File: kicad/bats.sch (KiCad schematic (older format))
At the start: 36 parts, among them P1 SERVO, SW1 UP, SW2 LEFT, SW3 DOWN, SW4 RIGHT, SW5 RESET, SW6 UP, SW7 LEFT, SW8 DOWN, SW9 RIGHT, U1 BUZZER

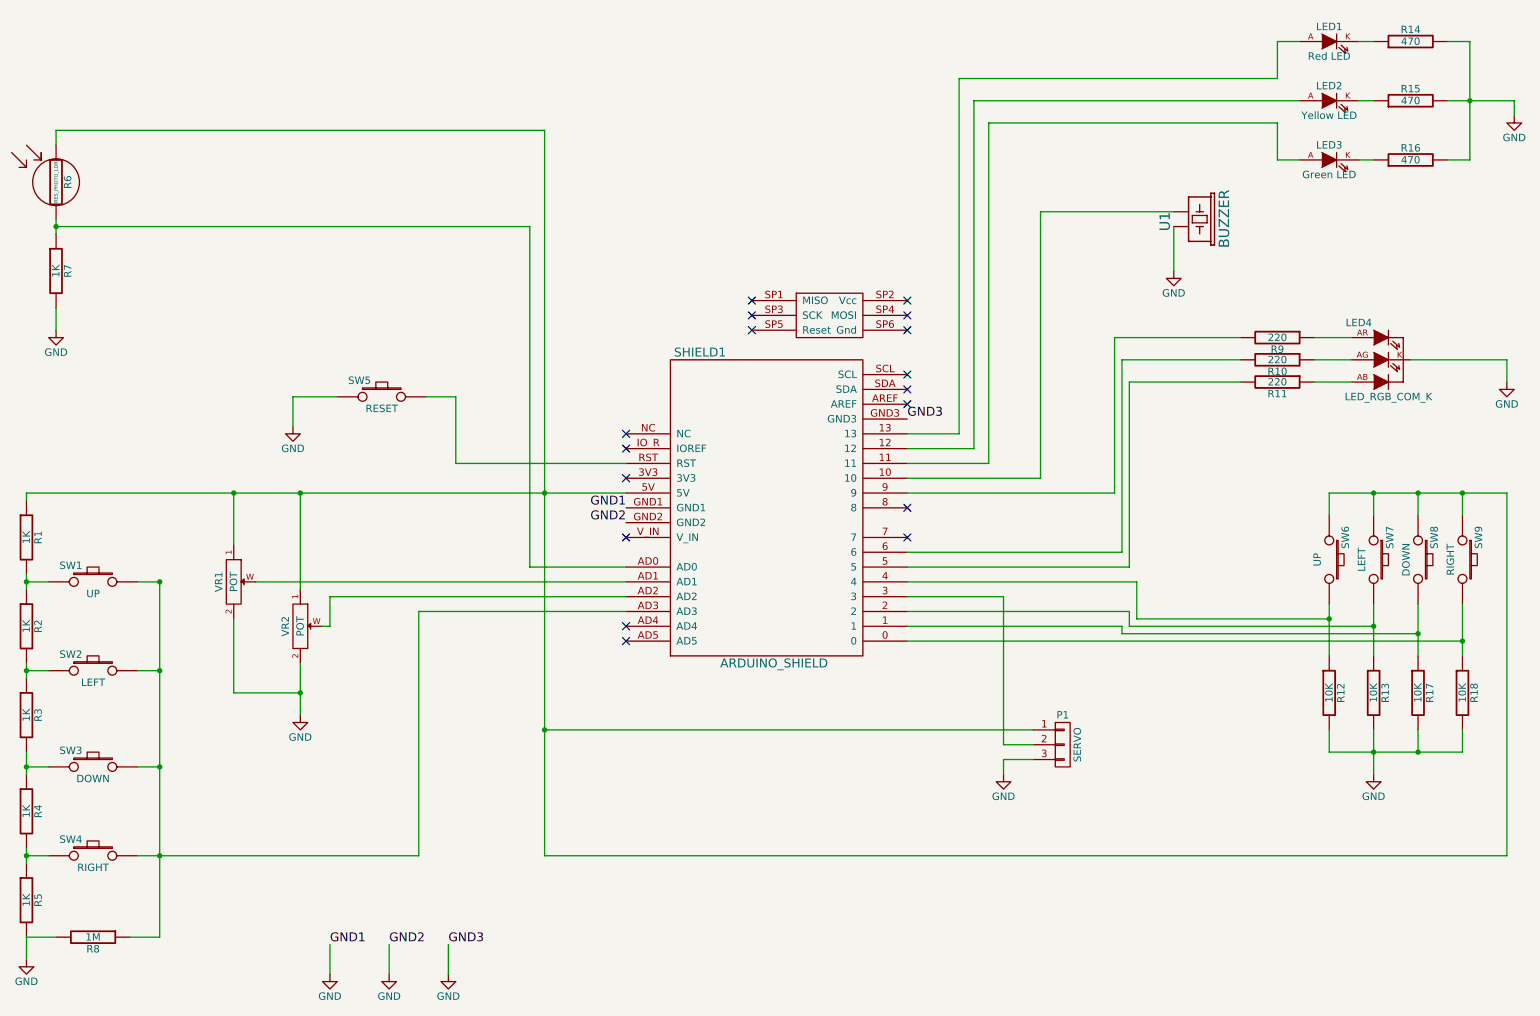
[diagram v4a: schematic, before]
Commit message: Cambiado o footprint dos potes. Todos os compoñentes situados na placa Mínimos cambios na documentación (engadida breve explicación dos submódulos de git)
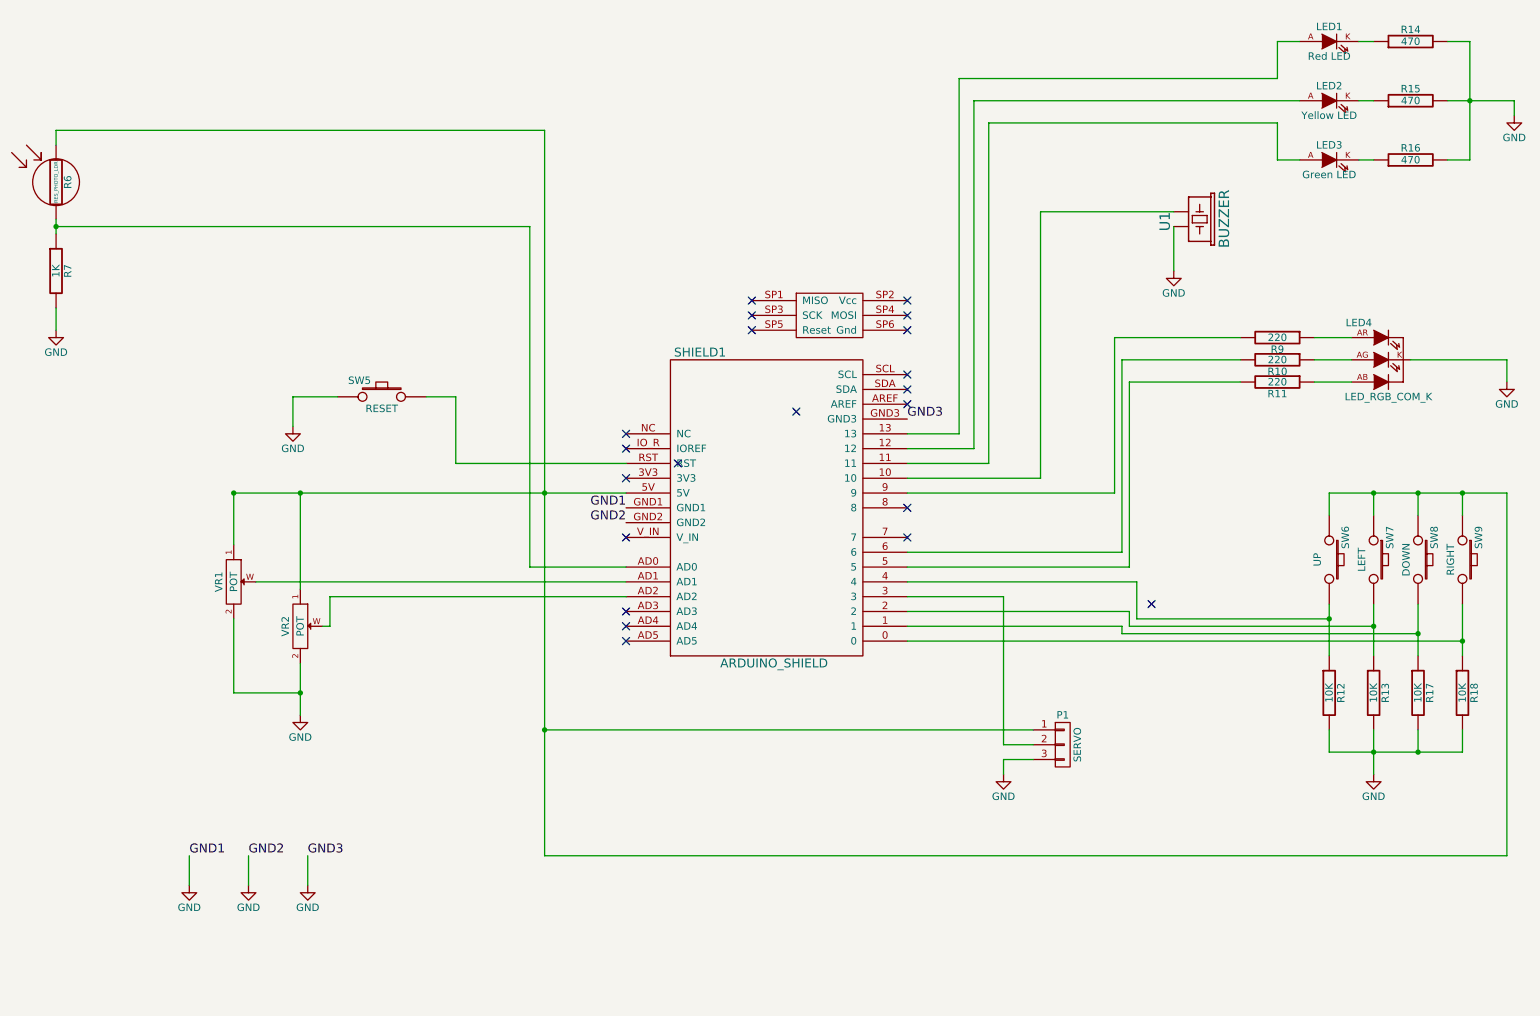
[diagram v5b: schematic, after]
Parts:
- removed R1, R2, R3, R4, R5: 1K, Resistors_ThroughHole:Resistor_Horizontal_RM10mm, symbol R
- removed R8: 1M, Resistors_ThroughHole:Resistor_Horizontal_RM10mm, symbol R
- removed SW1: UP, FT:SW_PUSHBUTTON_PTH, symbol SW_PUSHBUTTON
- removed SW2: LEFT, FT:SW_PUSHBUTTON_PTH, symbol SW_PUSHBUTTON
- removed SW3: DOWN, FT:SW_PUSHBUTTON_PTH, symbol SW_PUSHBUTTON
- removed SW4: RIGHT, FT:SW_PUSHBUTTON_PTH, symbol SW_PUSHBUTTON
- U1: footprint Buzzers_Beepers:MagneticBuzzer_StarMicronics_HMB-06_HMB-12 -> Buzzers_Beepers:MagneticBuzzer_Kingstate_KCG0601
- VR1, VR2: footprint (none) -> FT:POT_RV09_VERT
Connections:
- no-connect marks 17 -> 21

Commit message: Engadida unha "KiCAD cheat sheet", una chuleta para KiCAD, non rematada
Engadida unha segunda versión da placa intentando deixar todo nunha
cara.
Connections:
- no-connect marks 21 -> 18
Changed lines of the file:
@@
 $EndDescr
-$Comp
-L ARDUINO_SHIELD SHIELD1
-U 1 1 55897B99
-P 5800 4050
-F 0 "SHIELD1" H 5350 5200 60  0000 C CNN
-F 1 "ARDUINO_SHIELD" H 5850 3100 60  0000 C CNN
-F 2 "FT:ARDUINO_SHIELD" H 5800 3850 50  0001 C CNN
-F 3 "" H 5800 4050 60  0000 C CNN
-	1    5800 4050
-	1    0    0    -1
-$EndComp
 $Comp
 L LED LED3
@@
 $EndComp
 NoConn ~ 4850 4650
-NoConn ~ 8400 4600
-NoConn ~ 6000 3300
-NoConn ~ 5200 3650
+$Comp
+L ARDUINO_SHIELD SHIELD1
+U 1 1 55897B99
+P 5800 4050
+F 0 "SHIELD1" H 5350 5200 60  0000 C CNN
+F 1 "ARDUINO_SHIELD" H 5850 3100 60  0000 C CNN
+F 2 "FT:ARDUINO_SHIELD" H 5800 3850 50  0001 C CNN
+F 3 "" H 5800 4050 60  0000 C CNN
+	1    5800 4050
+	1    0    0    -1
+$EndComp
 $EndSCHEMATC

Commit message: Un commit intermedio facendo probas
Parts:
- added R1: 10K, Resistors_ThroughHole:Resistor_Horizontal_RM10mm, symbol R
- added SW1: SHOT, FT:SW_PUSHBUTTON_PTH, symbol SW_PUSHBUTTON
- renumbered SW5 to SW0, SW6 to SW2, SW7 to SW3, SW8 to SW4, SW9 to SW5
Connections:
- net GND: now also R1.2
- net ARD4: now reaches R18.1, SW5.2
- net ARD4: now also SHIELD1.4; no longer SHIELD1.0
- net ARD3: now reaches R17.1, SW4.2
- net ARD3: now also SHIELD1.3; no longer SHIELD1.1
- net ARD10: now reaches SHIELD1.10
- net ARD10: now also R10.2; no longer U1.2 (GND)
- net ARD11: now reaches SHIELD1.11
- net ARD11: now also R9.2; no longer LED3.A
- net at SHIELD1.12: no longer LED2.A
- net ARD13: now reaches SHIELD1.13
- net ARD13: now also U1.2 (GND); no longer LED1.A
- net ARD2: now reaches R13.1, SHIELD1.2, SW3.2
- net ARD5: now reaches P1.2 (P2)
- net ARD5: now also SHIELD1.5; no longer SHIELD1.3
- net ARD1: now reaches R12.1, SW2.2
- net ARD1: now also SHIELD1.1; no longer SHIELD1.4
- net ARD9: now reaches R11.2
- net ARD9: now also SHIELD1.9; no longer SHIELD1.5
- net at P1.1 (P1), R6.1, SHIELD1.5V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: now also SW1.1
- net ARD6: now reaches SHIELD1.6
- net ARD6: now also LED3.A; no longer R10.2
- net ARD7: now reaches SHIELD1.7
- net ARD7: now also LED2.A
- net ARD8: now reaches SHIELD1.8
- net ARD8: now also LED1.A
- new net ARD0: R1.1, SHIELD1.0, SW1.2
- no-connect marks 18 -> 17
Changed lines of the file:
@@
-$EndComp
-$Comp
-L SW_PUSHBUTTON SW6
-U 1 1 5589867E
-P 9600 4300
-F 0 "SW6" H 9450 4410 50  0000 C CNN
-F 1 "UP" H 9600 4220 50  0000 C CNN
-F 2 "FT:SW_PUSHBUTTON_PTH" H 9600 4300 60  0001 C CNN
-F 3 "" H 9600 4300 60  0000 C CNN
-	1    9600 4300
-	0    1    1    0
 $EndComp
 $Comp
@@
 $EndComp
 $Comp
-L SW_PUSHBUTTON SW7
+L SW_PUSHBUTTON SW3
 U 1 1 558AEB11
 P 9900 4300
-F 0 "SW7" H 9750 4410 50  0000 C CNN
+F 0 "SW3" H 9750 4410 50  0000 C CNN
 F 1 "LEFT" H 9900 4220 50  0000 C CNN
 F 2 "FT:SW_PUSHBUTTON_PTH" H 9900 4300 60  0001 C CNN
@@
 $EndComp
 $Comp
-L SW_PUSHBUTTON SW8
+L SW_PUSHBUTTON SW4
 U 1 1 558AEBB0
 P 10200 4300
-F 0 "SW8" H 10050 4410 50  0000 C CNN
+F 0 "SW4" H 10050 4410 50  0000 C CNN
 F 1 "DOWN" H 10200 4220 50  0000 C CNN
 F 2 "FT:SW_PUSHBUTTON_PTH" H 10200 4300 60  0001 C CNN
@@
 $EndComp
 $Comp
-L SW_PUSHBUTTON SW9
+L SW_PUSHBUTTON SW5
 U 1 1 558AEBBD
 P 10500 4300
-F 0 "SW9" H 10350 4410 50  0000 C CNN
+F 0 "SW5" H 10350 4410 50  0000 C CNN
 F 1 "RIGHT" H 10500 4220 50  0000 C CNN
 F 2 "FT:SW_PUSHBUTTON_PTH" H 10500 4300 60  0001 C CNN
@@
 $EndComp
 $Comp
-L SW_PUSHBUTTON SW5
+L SW_PUSHBUTTON SW0
 U 1 1 558B73E7
 P 3200 3200
-F 0 "SW5" H 3050 3310 50  0000 C CNN
+F 0 "SW0" H 3050 3310 50  0000 C CNN
 F 1 "RESET" H 3200 3120 50  0000 C CNN
 F 2 "FT:SW_PUSHBUTTON_PTH" H 3200 3200 60  0001 C CNN
@@
 	1    0    0    -1
 $EndComp
-NoConn ~ 6750 3950
-NoConn ~ 6750 4150
 NoConn ~ 4850 4750
 NoConn ~ 4850 4850
@@
 Connection ~ 10550 1200
 Wire Wire Line
-	9400 1600 9250 1600
-Wire Wire Line
-	7100 1050 7100 3450
-Wire Wire Line
-	7100 3450 6750 3450
-Wire Wire Line
-	7200 1200 9400 1200
-Wire Wire Line
-	7200 1200 7200 3550
-Wire Wire Line
-	7200 3550 6750 3550
-Wire Wire Line
-	7300 1350 7300 3650
-Wire Wire Line
-	7300 3650 6750 3650
-Wire Wire Line
 	1000 2600 1000 2750
 Wire Wire Line
@@
 Wire Wire Line
 	1000 1400 1000 1500
-Wire Wire Line
-	7650 1950 8550 1950
 Wire Wire Line
 	8550 2050 8550 2350
@@
 Connection ~ 10500 3850
 Wire Wire Line
-	9600 3850 10800 3850
+	9300 3850 10800 3850
 Wire Wire Line
 	9600 3850 9600 4000
-Connection ~ 9600 4700
-Connection ~ 9900 4750
-Connection ~ 10200 4800
-Connection ~ 10500 4850
 Wire Wire Line
 	9600 5450 9600 5600
 Wire Wire Line
-	9600 5600 10500 5600
+	9300 5600 10500 5600
 Wire Wire Line
 	10500 5600 10500 5450
@@
 Connection ~ 10200 5600
 Wire Wire Line
-	10500 4850 6750 4850
-Wire Wire Line
-	8200 4800 10200 4800
-Wire Wire Line
-	8200 4800 8200 4750
-Wire Wire Line
-	8200 4750 6750 4750
-Wire Wire Line
-	9900 4750 8250 4750
-Wire Wire Line
-	8250 4750 8250 4650
-Wire Wire Line
-	8250 4650 6750 4650
-Wire Wire Line
-	8300 4700 9600 4700
-Wire Wire Line
-	8300 4450 8300 4700
-Wire Wire Line
-	7300 1350 9250 1350
-Wire Wire Line
-	9250 1350 9250 1600
-Wire Wire Line
-	7100 1050 9250 1050
-Wire Wire Line
-	9250 1050 9250 800
-Wire Wire Line
-	9250 800  9400 800
-Wire Wire Line
 	9500 2800 9750 2800
 Wire Wire Line
@@
 Wire Wire Line
 	10850 1200 10850 1300
-Wire Wire Line
-	6750 3750 7650 3750
-Wire Wire Line
-	7650 3750 7650 1950
-Wire Wire Line
-	6750 3850 8150 3850
-Wire Wire Line
-	8150 3850 8150 2800
-Wire Wire Line
-	8150 2800 9000 2800
-Wire Wire Line
-	9000 2950 8200 2950
-Wire Wire Line
-	8200 2950 8200 4250
-Wire Wire Line
-	8200 4250 6750 4250
-Wire Wire Line
-	6750 4350 8250 4350
-Wire Wire Line
-	8250 4350 8250 3100
-Wire Wire Line
-	8250 3100 9000 3100
-Wire Wire Line
-	6750 4450 8300 4450
-Wire Wire Line
-	6750 4550 7400 4550
-Wire Wire Line
-	7400 4550 7400 5550
 Wire Wire Line
 	7400 5550 7600 5550
@@
 	1    0    0    -1
 $EndComp
+Wire Wire Line
+	8550 1950 8250 1950
+Text Label 8250 1950 2    60   ~ 0
+ARD13
+Text Label 6750 3450 0    60   ~ 0
+ARD13
+Wire Wire Line
+	9400 800  9000 800
+Wire Wire Line
+	9400 1200 9000 1200
+Wire Wire Line
+	9400 1600 9000 1600
+Text Label 6750 3650 0    60   ~ 0
+ARD11
+Text Label 6750 3750 0    60   ~ 0
+ARD10
+Text Label 6750 3850 0    60   ~ 0
+ARD9
+Wire Wire Line
+	9000 2800 8800 2800
+Wire Wire Line
+	9000 2950 8800 2950
+Wire Wire Line
+	9000 3100 8800 3100
+Text Label 8800 3100 2    60   ~ 0
+ARD9
+Text Label 8800 2950 2    60   ~ 0
+ARD10
+Text Label 8800 2800 2    60   ~ 0
+ARD11
+Text Label 9000 1200 2    60   ~ 0
+ARD7
+Text Label 9000 800  2    60   ~ 0
+ARD8
+Text Label 9000 1600 2    60   ~ 0
+ARD6
+Text Label 6750 4250 0    60   ~ 0
+ARD6
+Text Label 6750 4150 0    60   ~ 0
+ARD7
+Text Label 6750 3950 0    60   ~ 0
+ARD8
+NoConn ~ 6750 3550
+Text Label 6750 4350 0    60   ~ 0
+ARD5
+Text Label 7400 5550 2    60   ~ 0
+ARD5
+$Comp
+L SW_PUSHBUTTON SW1
+U 1 1 562027CC
+P 9300 4300
+F 0 "SW1" H 9150 4410 50  0000 C CNN
+F 1 "SHOT" H 9300 4220 50  0000 C CNN
+F 2 "FT:SW_PUSHBUTTON_PTH" H 9300 4300 60  0001 C CNN
+F 3 "" H 9300 4300 60  0000 C CNN
+	1    9300 4300
+	0    1    1    0
+$EndComp
+$Comp
+L R R1
+U 1 1 56202A0F
+P 9300 5200
+F 0 "R1" V 9380 5200 50  0000 C CNN
+F 1 "10K" V 9300 5200 50  0000 C CNN
+F 2 "Resistors_ThroughHole:Resistor_Horizontal_RM10mm" H 9300 5200 60  0001 C CNN
+F 3 "" H 9300 5200 60  0000 C CNN
+	1    9300 5200
+	1    0    0    -1
+$EndComp
+Wire Wire Line
+	9300 4600 9300 4950
+Wire Wire Line
+	9300 4000 9300 3850
+Connection ~ 9600 3850
+Wire Wire Line
+	9300 5450 9300 5600
+Connection ~ 9600 5600
+Text Label 6750 4850 0    60   ~ 0
+ARD0
+Text Label 6750 4750 0    60   ~ 0
+ARD1
+Text Label 6750 4650 0    60   ~ 0
+ARD2
+Text Label 6750 4550 0    60   ~ 0
+ARD3
+Text Label 6750 4450 0    60   ~ 0
+ARD4
+Connection ~ 10500 4650
+Wire Wire Line
+	10500 4650 8950 4650
+Text Label 8950 4650 2    60   ~ 0
+ARD4
+Connection ~ 10200 4700
+Wire Wire Line
+	10200 4700 8700 4700
+Text Label 8700 4700 2    60   ~ 0
+ARD3
+Connection ~ 9900 4750
+Wire Wire Line
+	9900 4750 8450 4750
+Text Label 8450 4750 2    60   ~ 0
+ARD2
+Connection ~ 9600 4800
+Wire Wire Line
+	9600 4800 8200 4800
+Text Label 8200 4800 2    60   ~ 0
+ARD1
+Connection ~ 9300 4850
+Wire Wire Line
+	9300 4850 7950 4850
+Text Label 7950 4850 2    60   ~ 0
+ARD0
+$Comp
+L SW_PUSHBUTTON SW2
+U 1 1 5589867E
+P 9600 4300
+F 0 "SW2" H 9450 4410 50  0000 C CNN
+F 1 "UP" H 9600 4220 50  0000 C CNN
+F 2 "FT:SW_PUSHBUTTON_PTH" H 9600 4300 60  0001 C CNN
+F 3 "" H 9600 4300 60  0000 C CNN
+	1    9600 4300
+	0    1    1    0
+$EndComp
 $EndSCHEMATC

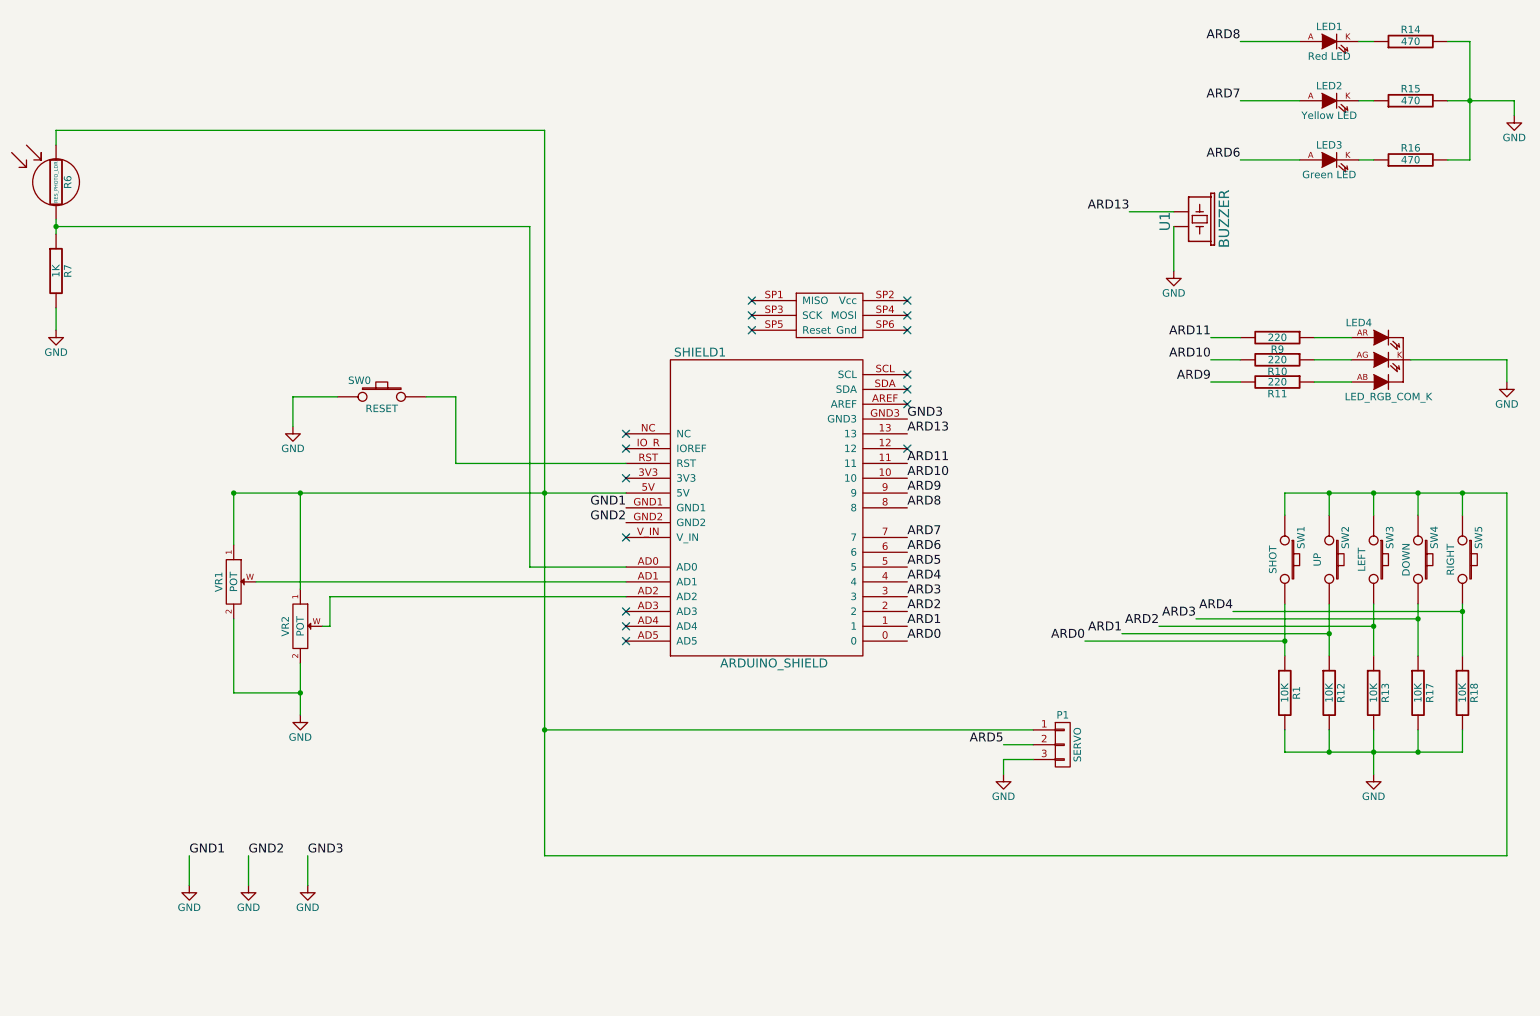
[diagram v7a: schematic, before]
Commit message: Recolocados casi todos os compoñentes Simplificado esquema Aumentado o ancho de pistas
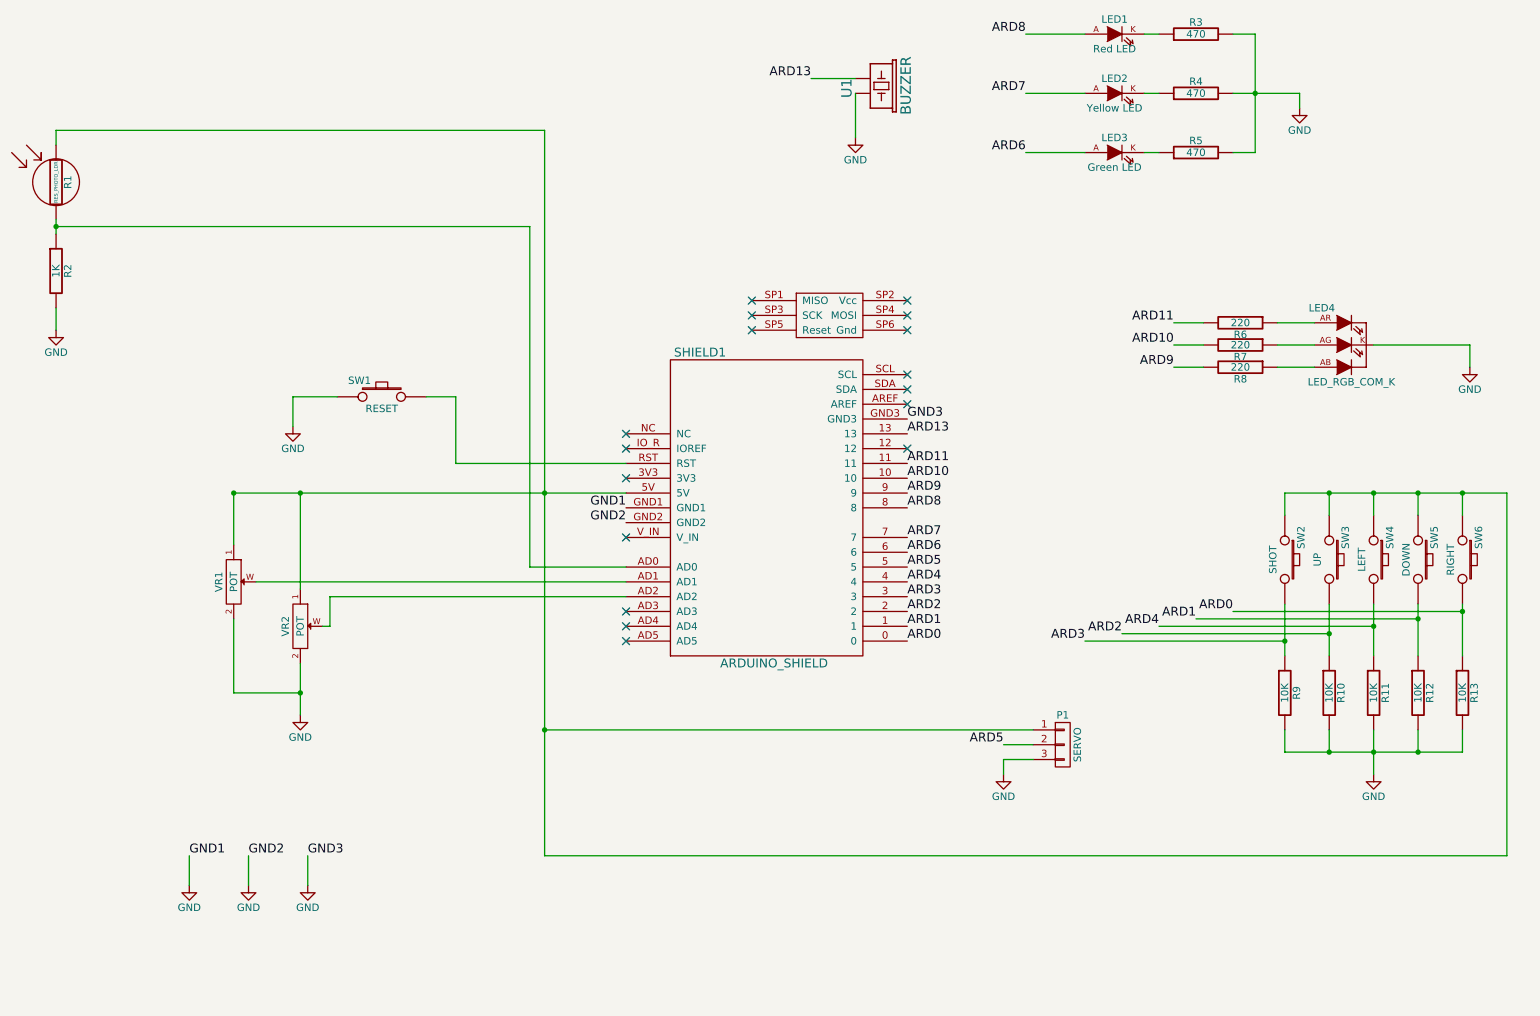
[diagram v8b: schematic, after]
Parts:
- renumbered R6 to R1, R12 to R10, R13 to R11, R17 to R12, R18 to R13, R7 to R2, R14 to R3, R15 to R4, R16 to R5, R9 to R6, R10 to R7, R11 to R8, R1 to R9, SW0 to SW1, SW1 to SW2, SW2 to SW3, SW3 to SW4, SW4 to SW5, SW5 to SW6
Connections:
- net ARD0: now also R13.1, SW6.2; no longer R9.1, SW2.2
- net ARD1: now also R12.1, SW5.2; no longer R10.1, SW3.2
- net ARD2: now also R10.1, SW3.2; no longer R11.1, SW4.2
- net ARD3: now also R9.1, SW2.2; no longer R12.1, SW5.2
- net ARD4: now also R11.1, SW4.2; no longer R13.1, SW6.2
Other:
- moved on the sheet: LED1, LED2, LED3, LED4, R3, R4, R5, R6, R7, R8, U1
